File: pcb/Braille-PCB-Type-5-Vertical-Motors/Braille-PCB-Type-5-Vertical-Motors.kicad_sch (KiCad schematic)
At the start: 39 parts, among them J1 Screw_Terminal_01x02, J2 Screw_Terminal_01x02, J21 Conn_01x05, J22 Conn_01x05, J23 Conn_01x05, J24 Conn_01x05, J3 Screw_Terminal_01x02, J4 Conn_01x03, J5 Conn_01x02, J6 Conn_01x08, J7 Jumper-3-Way-Power, J8 Barrel_Jack_Switch, SW1 SW_Push, SW2 SW_Push, U1 RP2040-Zero, U32 AMS1117-3.3

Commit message: PCB: Work on new revision
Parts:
- removed J4: Conn_01x03, Connector_PinHeader_2.54mm:PinHeader_1x03_P2.54mm_Vertical, symbol Connector_Generic:Conn_01x03
- removed J7: Jumper-3-Way-Power, 00-project-footprints:Jumper-3-Way-2.54mm-Headers, symbol 00-project-symbols:Jumper-3-Way-Power
- removed J8: Barrel_Jack_Switch, Connector_BarrelJack:BarrelJack_Horizontal, symbol Connector:Barrel_Jack_Switch
- removed JP1: Jumper_3_Open, Connector_PinHeader_2.54mm:PinHeader_1x03_P2.54mm_Vertical, symbol Jumper:Jumper_3_Open
- added C103: 100n, Capacitor_SMD:C_0603_1608Metric_Pad1.08x0.95mm_HandSolder, symbol Device:C
- added R103: R, Resistor_SMD:R_1206_3216Metric_Pad1.30x1.75mm_HandSolder, symbol Device:R
- added R105, R106: 5k1, Resistor_SMD:R_0603_1608Metric_Pad0.98x0.95mm_HandSolder, symbol Device:R
- added U103: INA219AxD, Package_SO:SOIC-8_3.9x4.9mm_P1.27mm, symbol Sensor_Energy:INA219AxD
- renumbered C1 to C101, C26 to C102, C28 to C104, C29 to C105, D27 to D101, D26 to D102, D1 to D103, H1 to H101, H2 to H102, H3 to H103, H4 to H104, H5 to H105, H9 to H106, H6 to H107, H10 to H108, H7 to H109, H8 to H110, H11 to H111, H12 to H112, J5 to J101, J1 to J102, J2 to J103, J3 to J104, J21 to J105, J22 to J106, J6 to J107, J23 to J108, J24 to J109, R51 to R101, R50 to R102, R1 to R104, SW1 to SW101, SW2 to SW102, U1 to U101, U32 to U102
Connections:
- net +3V3: now also C103.1, R105.1, R106.1, U103.5 (VS)
- net +5V: now also C104.1, U102.3 (VI)
- net GND: now also C103.2, U103.1 (A1), U103.2 (A0), U103.6 (GND)
- net VDC: now also J104.1 (Pin_1), R103.2, U103.7 (IN-)
- net at C105.1, U102.2 (VO): now also R103.1, U103.8 (IN+)
- net I2C_SCL: now reaches U101.8 (GP15)
- net I2C_SCL: now also R105.2, U103.4 (SCL)
- net I2C_SDA: now reaches U101.9 (GP14)
- net I2C_SDA: now also R106.2, U103.3 (SDA)
- no-connect marks 23 -> 24
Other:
- note added: "M2 Around Lights"
- note added: "Regulator for VDC Motor Drive"
- note removed: "Barrel Jack Center-Pos 5.5 OD x 2.1mm ID"
- note removed: "Optional Power Input"
- note removed: "Power Input and Selection"
- moved on the sheet: C104, C105, D103, H105, H106, H107, H108, H109, H110, H111, H112, J104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

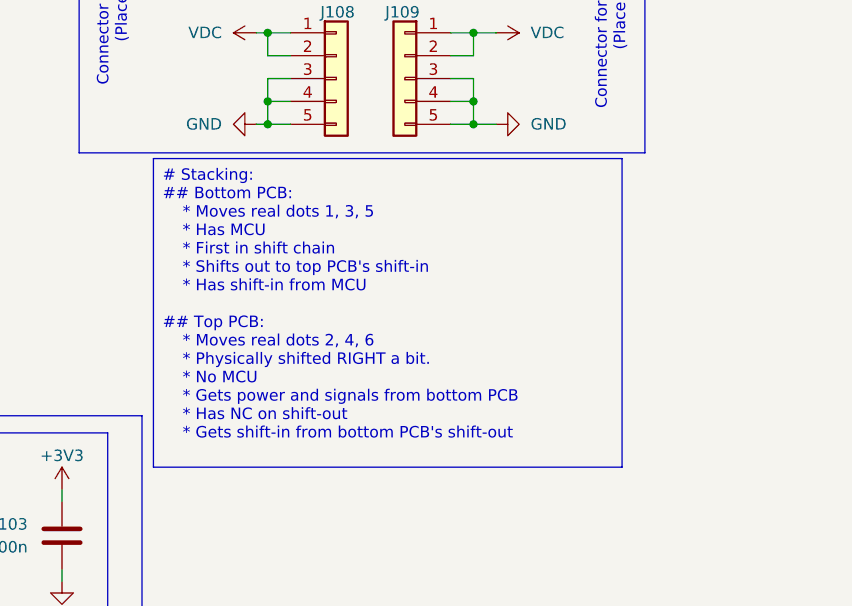
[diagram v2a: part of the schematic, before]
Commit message: pcb: Bump to KiCAD v9
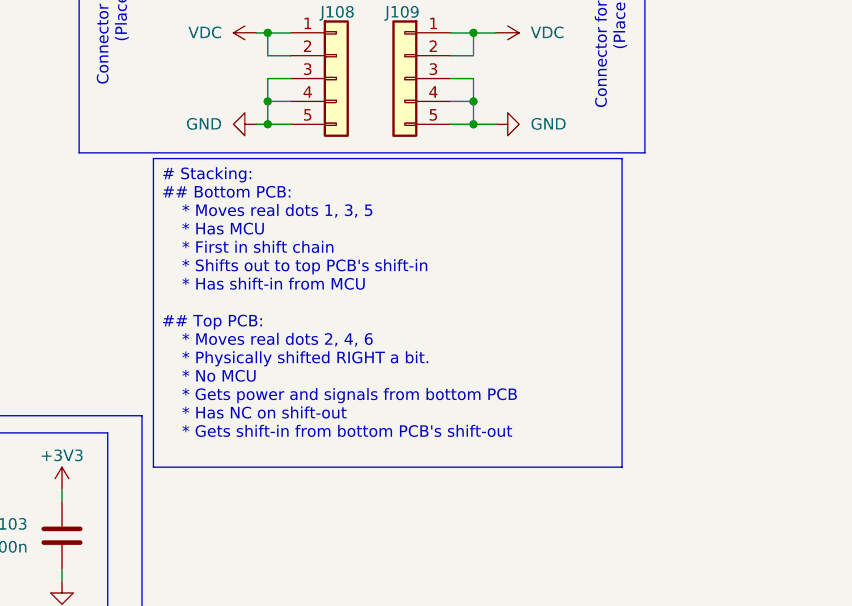
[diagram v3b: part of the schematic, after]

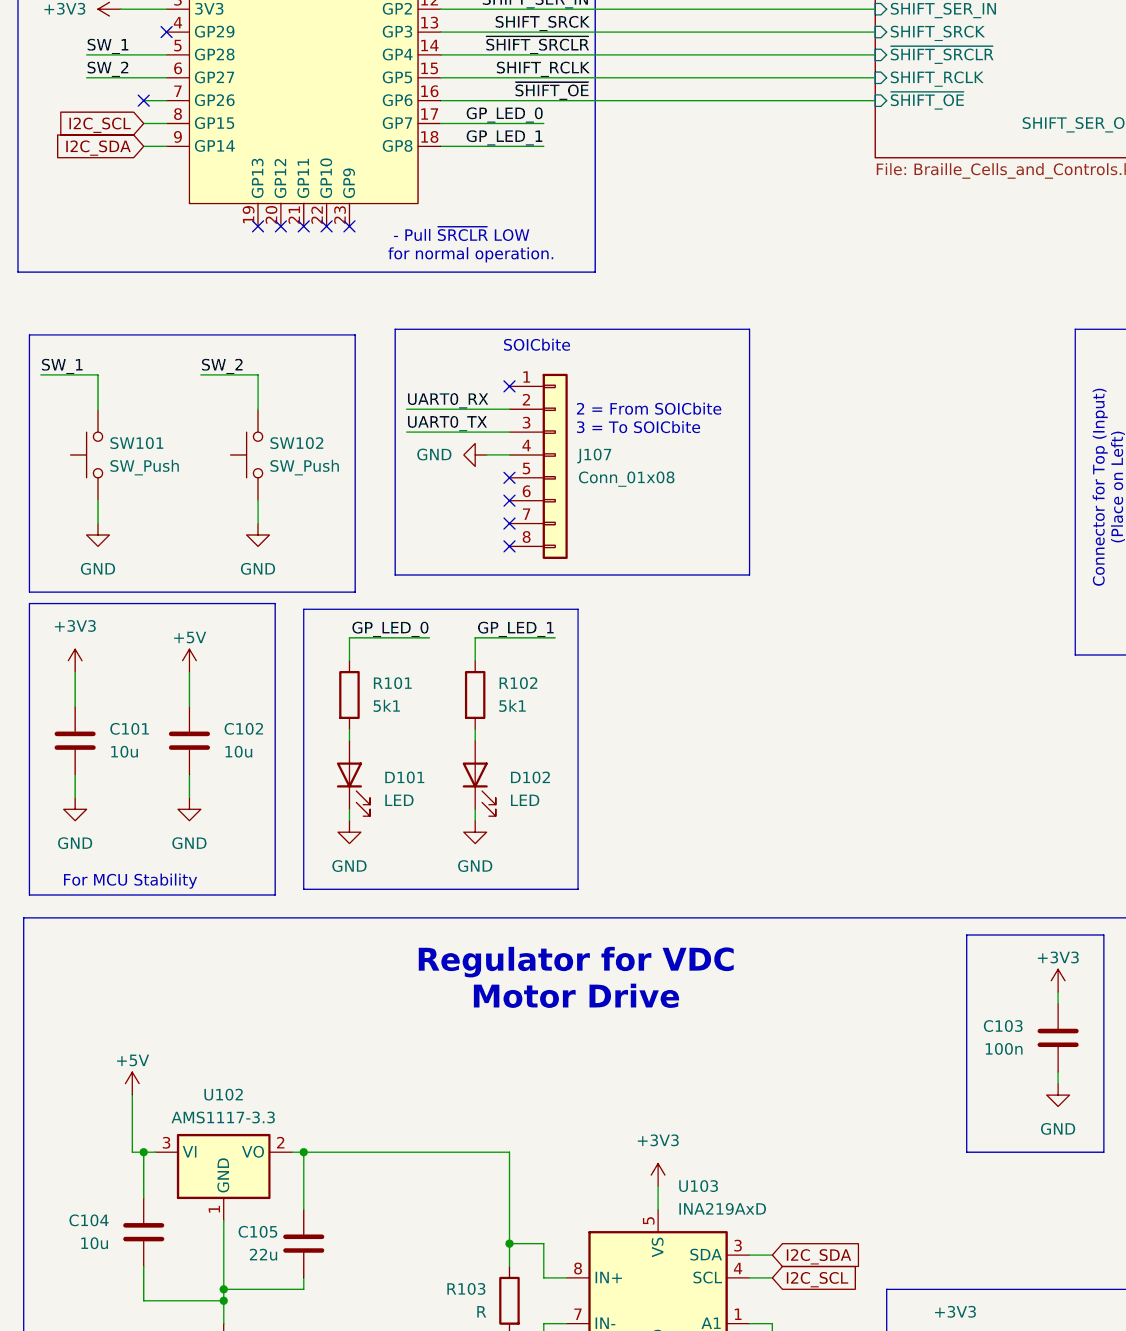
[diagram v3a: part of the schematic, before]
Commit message: pcb: Add I2C address comments
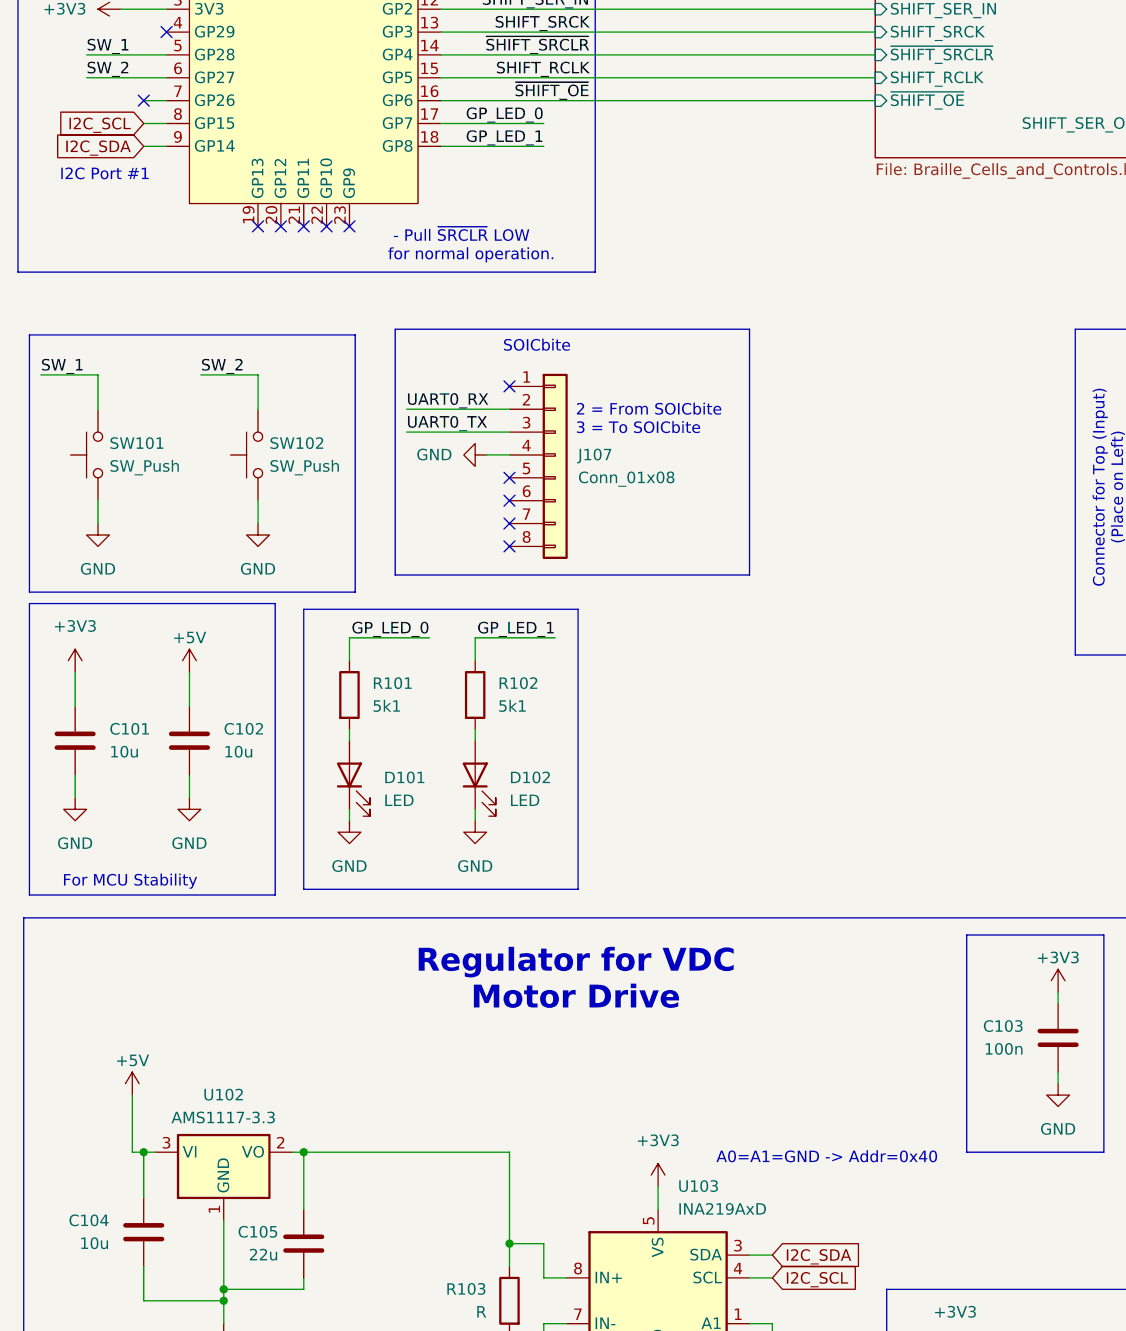
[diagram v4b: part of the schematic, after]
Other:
- note added: "A0=A1=GND -> Addr=0x40"
- note added: "I2C Port #1"
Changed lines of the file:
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@@
+		)
+	)
+	(text "A0=A1=GND -> Addr=0x40"
+		(exclude_from_sim no)
+		(at 103.886 158.242 0)
+		(effects
+			(font
+				(size 1.27 1.27)
+			)
+		)
+	)
+	(text "I2C Port #1"
+		(exclude_from_sim no)
+		(at 23.622 49.022 0)
+		(effects
+			(font
+				(size 1.27 1.27)
+			)
 		)
 	)

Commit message: chore: bump KiCAD to v9, maybe other minor changes
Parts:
- removed SW101, SW102: SW_Push, 00-project-footprints:PushButtonSMD_2.93x3.9, symbol Switch:SW_Push
- added S1, S2: Tactile Button, 160gf, PCM_JLCPCB:SW-SMD_4P-L5.1-W5.1-P3.70-LS6.5-TL-2, symbol PCM_JLCPCB-Connectors_Buttons:Tactile Button, 160gf
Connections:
- net GND: now also S1.3 (C), S1.4 (D), S2.3 (C), S2.4 (D)
- net SW_1: now also S1.1 (A), S1.2 (B)
- net SW_2: now also S2.1 (A), S2.2 (B)
